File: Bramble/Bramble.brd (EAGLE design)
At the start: 84.8 x 55.9 mm, 15 parts

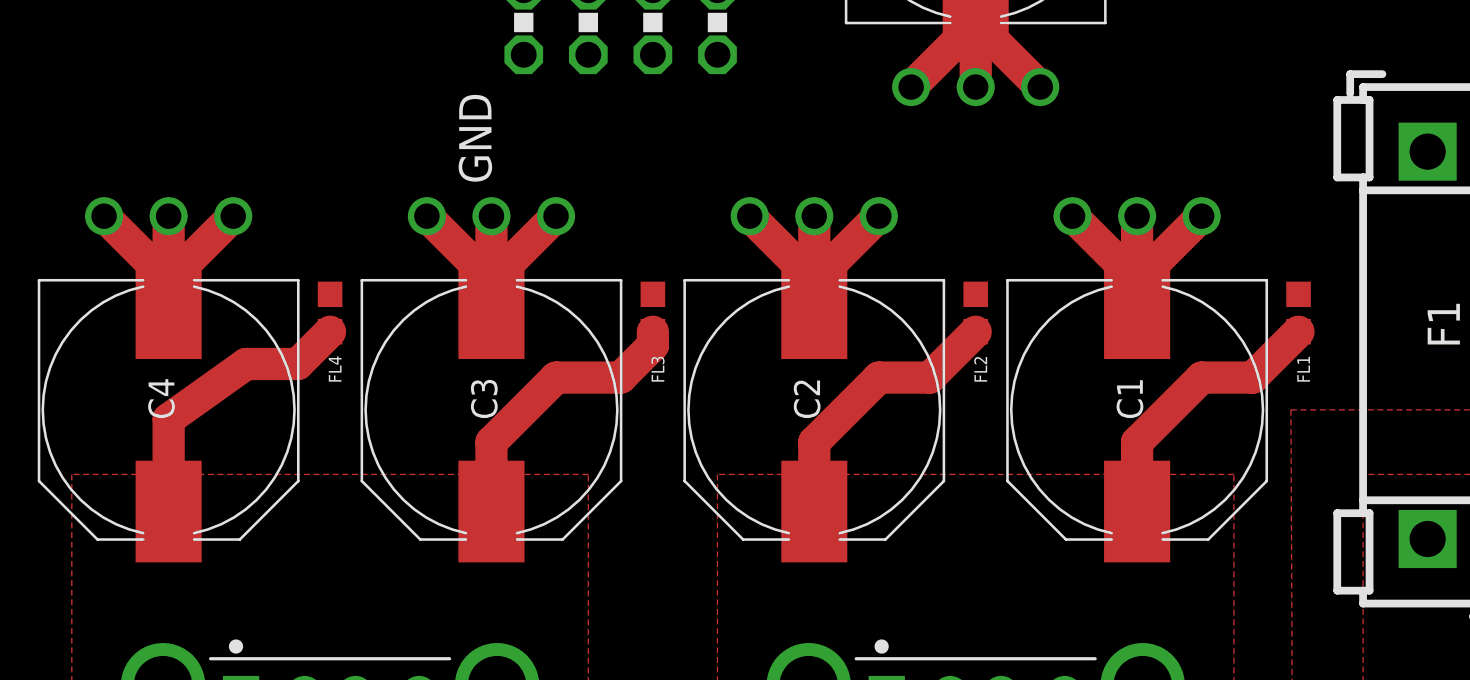
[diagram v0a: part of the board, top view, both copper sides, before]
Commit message: Altered ferite beed position
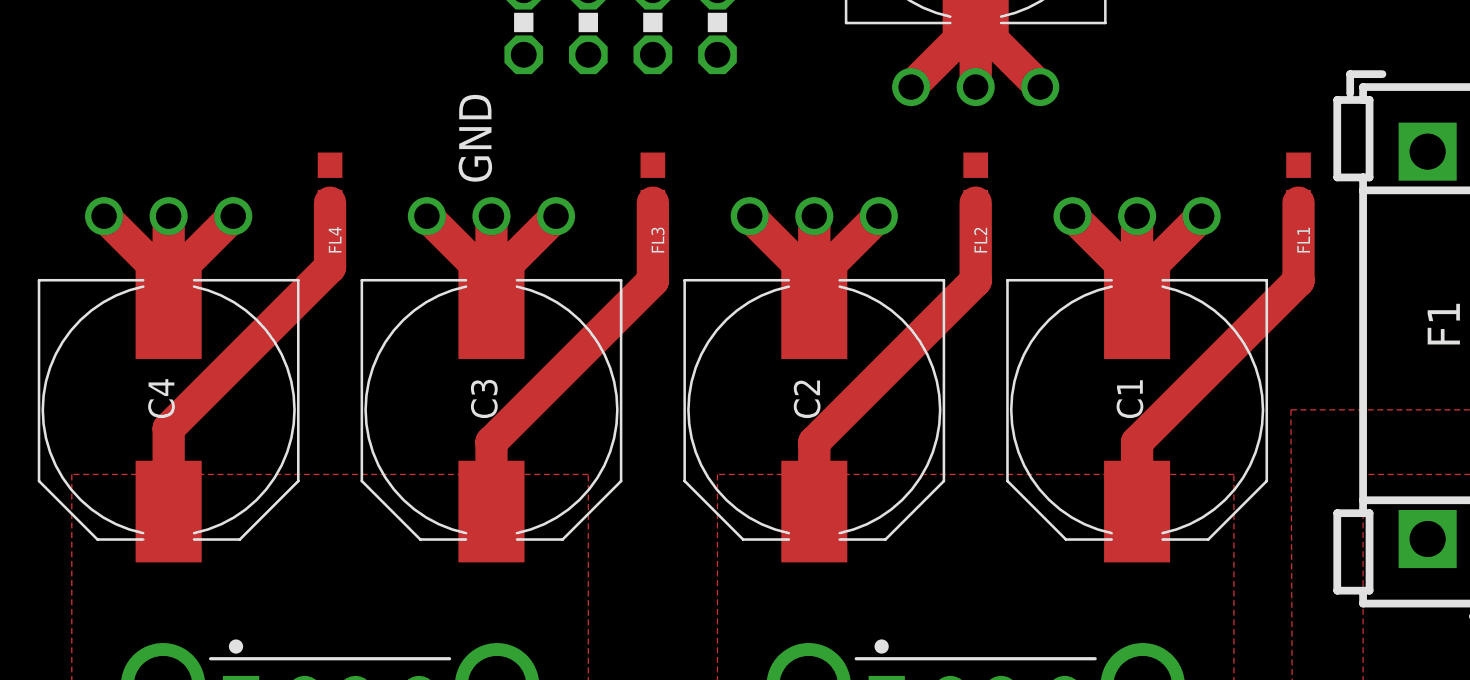
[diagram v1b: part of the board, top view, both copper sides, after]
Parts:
- moved FL1 5.08 mm to (55.9, 36.8)
- moved FL2 5.08 mm to (43.2, 36.8)
- moved FL3 5.08 mm to (30.5, 36.8)
- moved FL4 5.08 mm to (17.8, 36.8)
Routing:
- net 5VOUT12: track 23.2 -> 31.0 mm
- net 5VOUT34: track 22.4 -> 29.6 mm

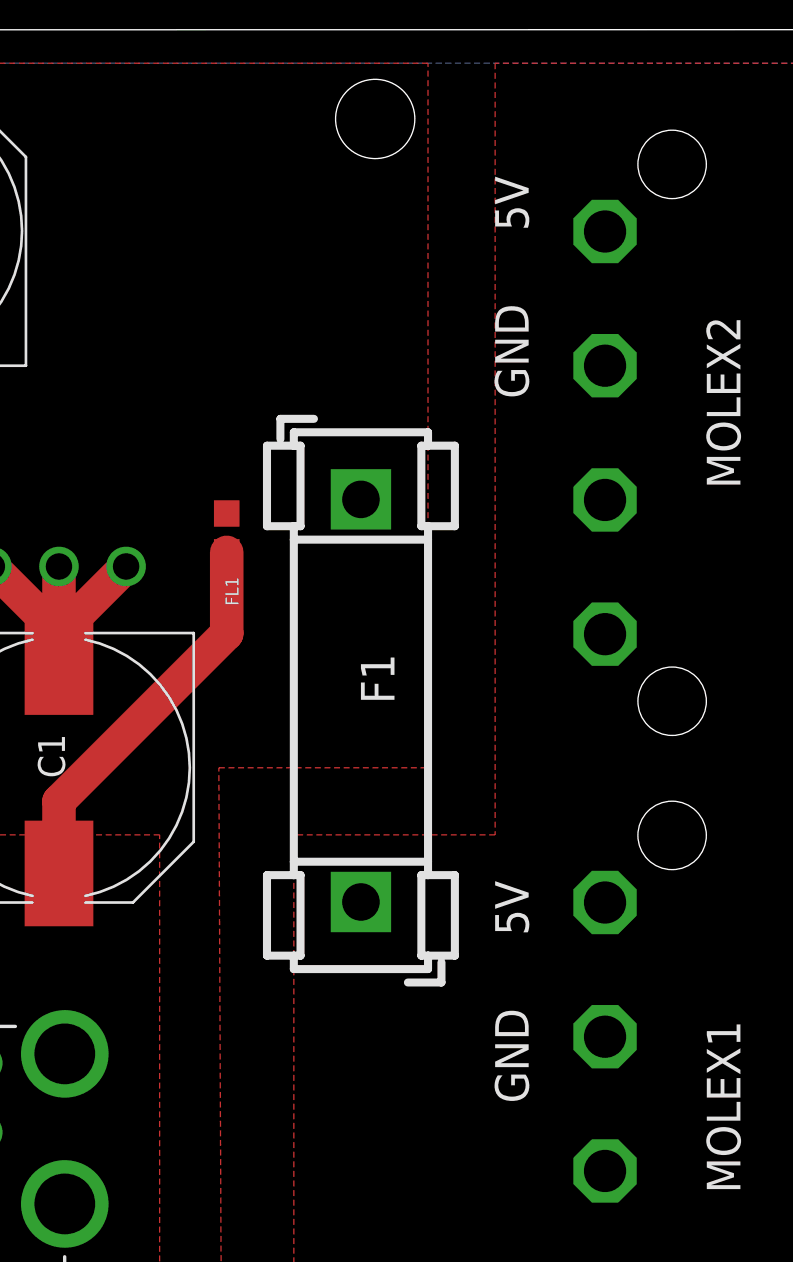
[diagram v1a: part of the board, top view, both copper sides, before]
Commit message: Updated fuse holder
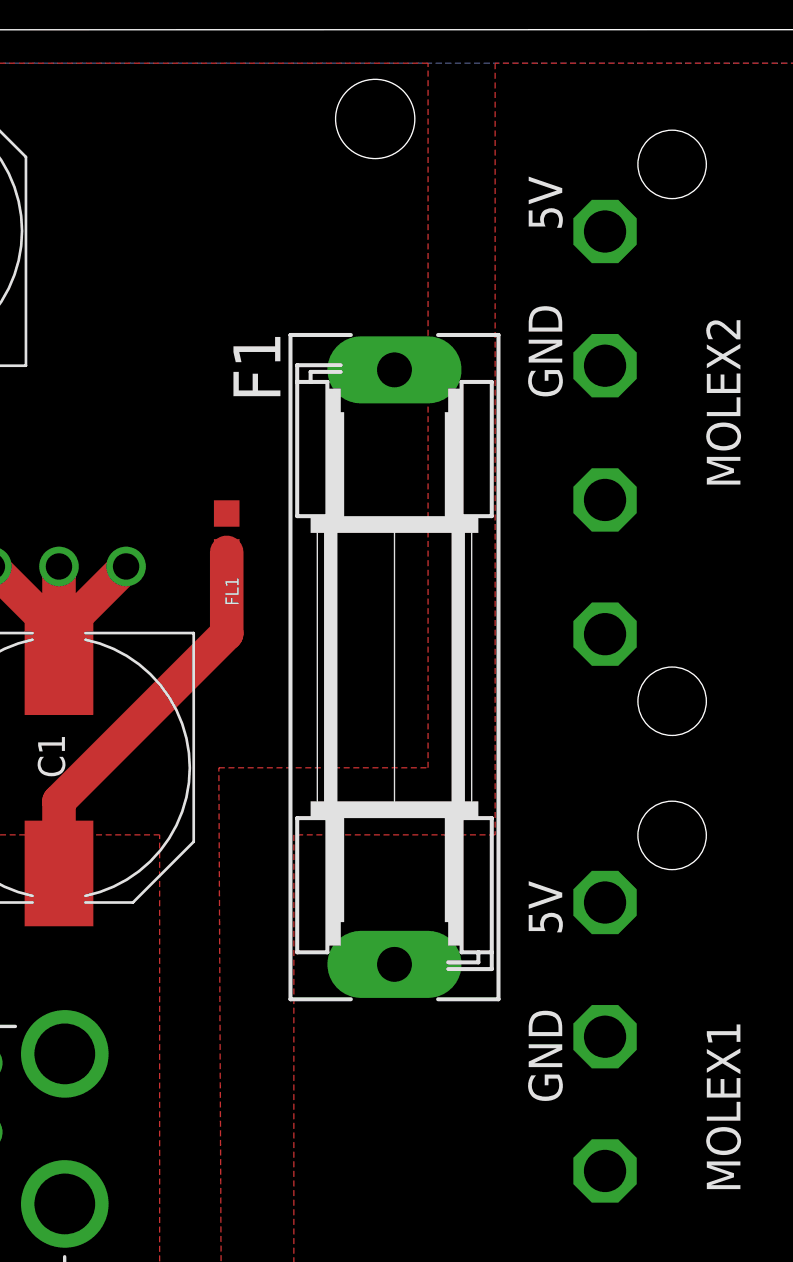
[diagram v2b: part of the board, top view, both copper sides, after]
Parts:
- F1: value FUSEBLANK_5X20MM -> FUSESH22,5; device fuse:FUSE_HOLDER_5X20MM -> fuse:SH22,5
- moved F1 6.48 mm to (62.2, 31.8)
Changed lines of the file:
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@@
 <hole x="61.5" y="52.5" drill="3"/>
 <hole x="61.5" y="3.5" drill="3"/>
-<text x="67.31" y="21.59" size="1.27" layer="25" rot="R90">5V</text>
-<text x="67.31" y="15.24" size="1.27" layer="25" rot="R90">GND</text>
+<text x="68.58" y="21.59" size="1.27" layer="25" rot="R90">5V</text>
+<text x="68.58" y="15.24" size="1.27" layer="25" rot="R90">GND</text>
 <text x="24.13" y="36.83" size="1.27" layer="25" rot="R90">GND</text>
 <text x="22.86" y="46.99" size="1.27" layer="25" rot="R270">5V</text>
-<text x="67.31" y="48.26" size="1.27" layer="25" rot="R90">5V</text>
-<text x="67.31" y="41.91" size="1.27" layer="25" rot="R90">GND</text>
+<text x="68.58" y="48.26" size="1.27" layer="25" rot="R90">5V</text>
+<text x="68.58" y="41.91" size="1.27" layer="25" rot="R90">GND</text>
 </plain>
 <attributes>
@@
 </autorouter>
 <elements>
-<element name="F1" library="fuse" library_urn="urn:adsk.eagle:library:233" package="FUSE_HOLDER_5X20MM" package3d_urn="urn:adsk.eagle:package:14079/1" value="FUSEBLANK_5X20MM" x="60.96" y="38.1" smashed="yes" rot="R270">
-<attribute name="MF" value="" x="60.96" y="38.1" size="1.778" layer="27" rot="R270" display="off"/>
-<attribute name="MPN" value="" x="60.96" y="38.1" size="1.778" layer="27" rot="R270" display="off"/>
-<attribute name="NAME" x="60.96" y="32.258" size="1.27" layer="25" rot="R270"/>
-<attribute name="OC_FARNELL" value="unknown" x="60.96" y="38.1" size="1.778" layer="27" rot="R270" display="off"/>
-<attribute name="OC_NEWARK" value="unknown" x="60.96" y="38.1" size="1.778" layer="27" rot="R270" display="off"/>
-<attribute name="POPULARITY" value="4" x="60.96" y="38.1" size="1.778" layer="27" rot="R270" display="off"/>
-</element>
 <element name="JP1" library="Connector" library_urn="urn:adsk.eagle:library:16378166" package="2X04/90" package3d_urn="urn:adsk.eagle:package:22465/2" value="PINHD-2X4/90" x="29.21" y="48.26" smashed="yes">
 <attribute name="CATEGORY" value="CONNECTOR" x="29.21" y="48.26" size="1.778" layer="27" display="off"/>
@@
 <attribute name="PRICE" value="None" x="17.78" y="11.43" size="1.778" layer="27" display="off"/>
 <attribute name="PURCHASE-URL" value="https://pricing.snapeda.com/search/part/5787745-1/?ref=eda" x="17.78" y="11.43" size="1.778" layer="27" display="off"/>
+</element>
+<element name="F1" library="fuse" library_urn="urn:adsk.eagle:library:233" package="SH22,5" package3d_urn="urn:adsk.eagle:package:14059/1" value="FUSESH22,5" x="62.23" y="31.75" smashed="yes" rot="R270">
+<attribute name="MF" value="" x="62.23" y="31.75" size="1.778" layer="27" rot="R270" display="off"/>
+<attribute name="MPN" value="" x="62.23" y="31.75" size="1.778" layer="27" rot="R270" display="off"/>
+<attribute name="NAME" x="56.134" y="44.45" size="1.778" layer="25" ratio="10" rot="R270"/>
+<attribute name="OC_FARNELL" value="unknown" x="62.23" y="31.75" size="1.778" layer="27" rot="R270" display="off"/>
+<attribute name="OC_NEWARK" value="unknown" x="62.23" y="31.75" size="1.778" layer="27" rot="R270" display="off"/>
+<attribute name="POPULARITY" value="8" x="62.23" y="31.75" size="1.778" layer="27" rot="R270" display="off"/>
 </element>
 </elements>
@@
 </signal>
 <signal name="5VIN">
-<contactref element="F1" pad="2"/>
 <contactref element="MOLEX1" pad="1"/>
 <contactref element="MOLEX2" pad="1"/>
@@
 <vertex x="82.55" y="54.61"/>
 </polygon>
+<contactref element="F1" pad="2"/>
 </signal>
 <signal name="5VOUT12">

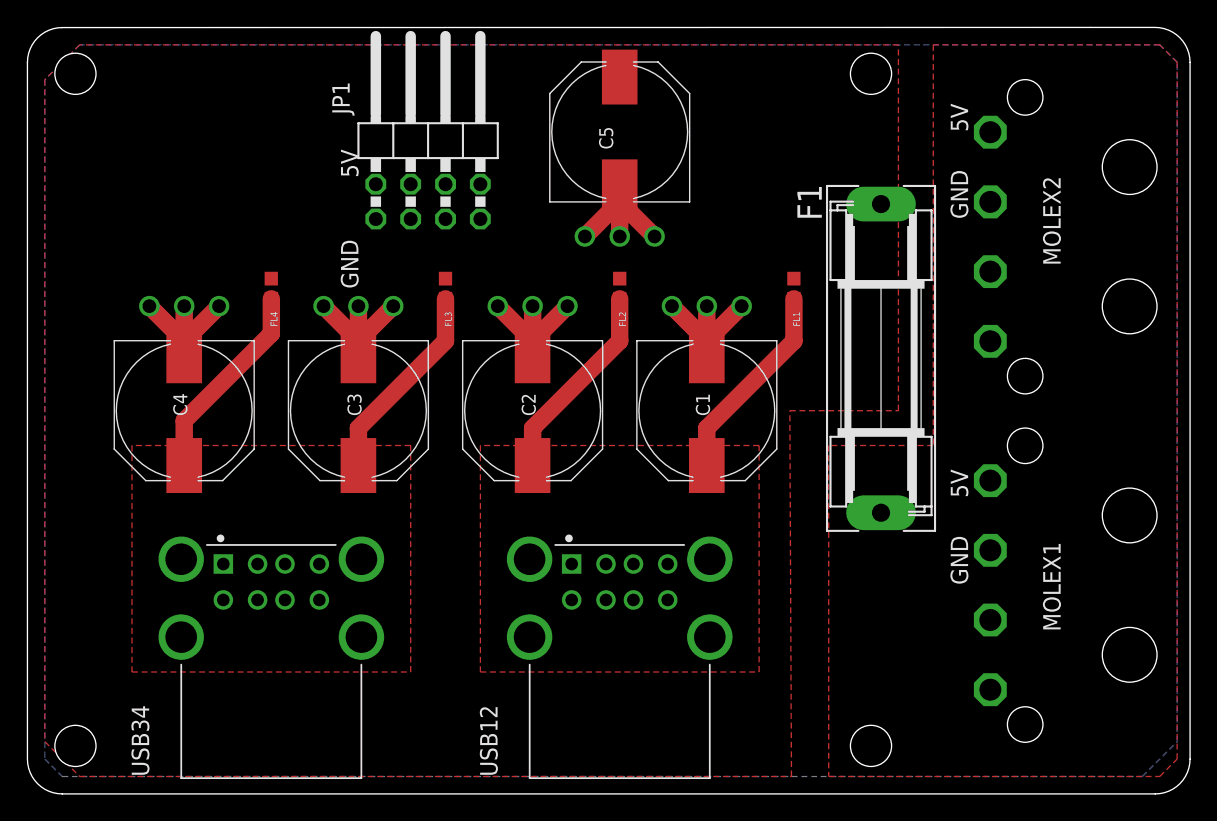
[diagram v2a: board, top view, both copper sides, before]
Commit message: Parts position tweaks
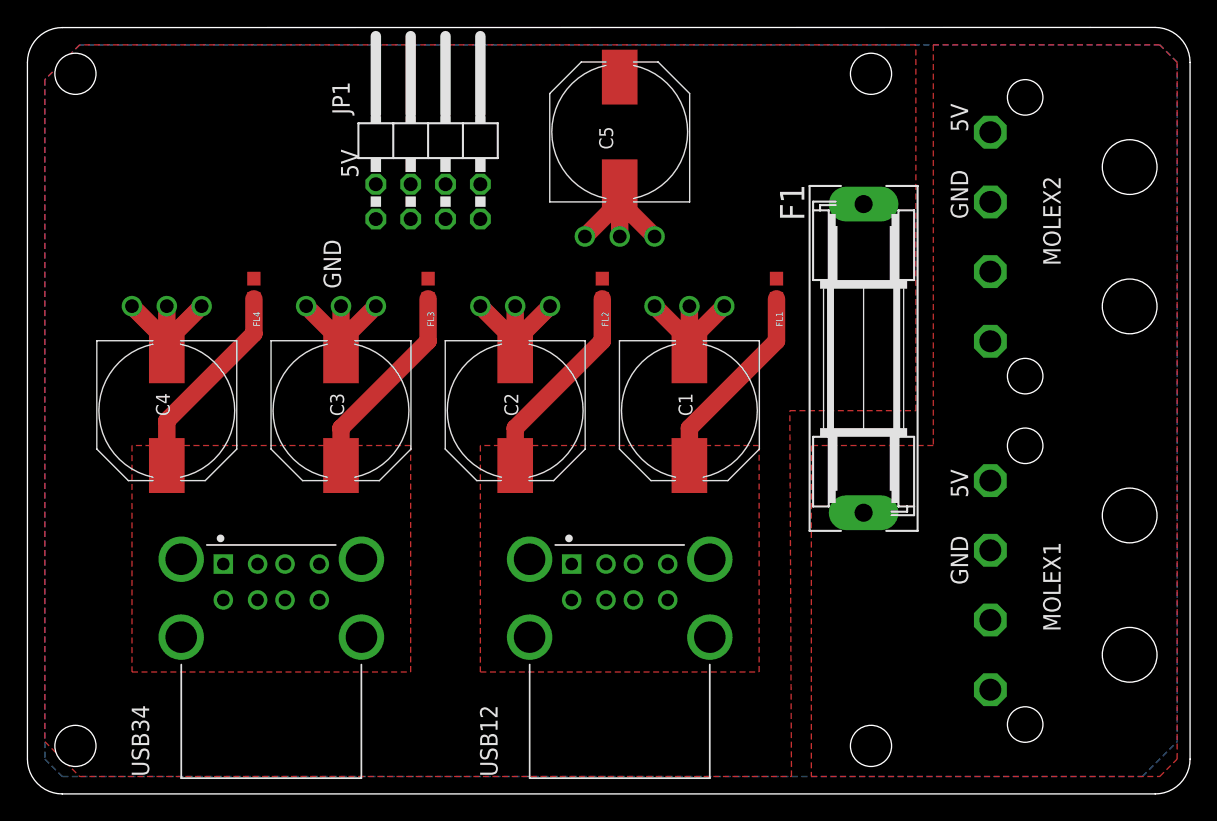
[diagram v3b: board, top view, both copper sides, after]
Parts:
- moved C1 1.27 mm to (48.3, 27.9)
- moved FL1 1.27 mm to (54.6, 36.8)
- moved FL2 1.27 mm to (41.9, 36.8)
- moved C3 1.27 mm to (22.9, 27.9)
- moved C4 1.27 mm to (10.2, 27.9)
- moved FL3 1.27 mm to (29.2, 36.8)
- moved FL4 1.27 mm to (16.5, 36.8)
- moved C2 1.27 mm to (35.6, 27.9)
- moved F1 1.27 mm to (61.0, 31.8)
